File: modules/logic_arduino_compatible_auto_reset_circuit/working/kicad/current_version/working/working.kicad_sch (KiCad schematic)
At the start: 2 parts

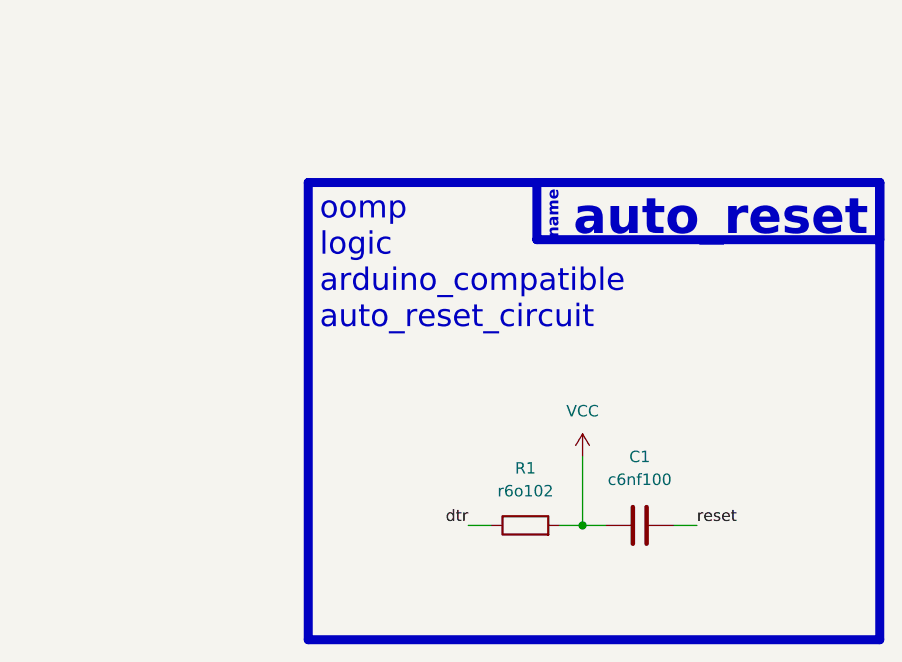
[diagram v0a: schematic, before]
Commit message: fixed formatting to be more consistent
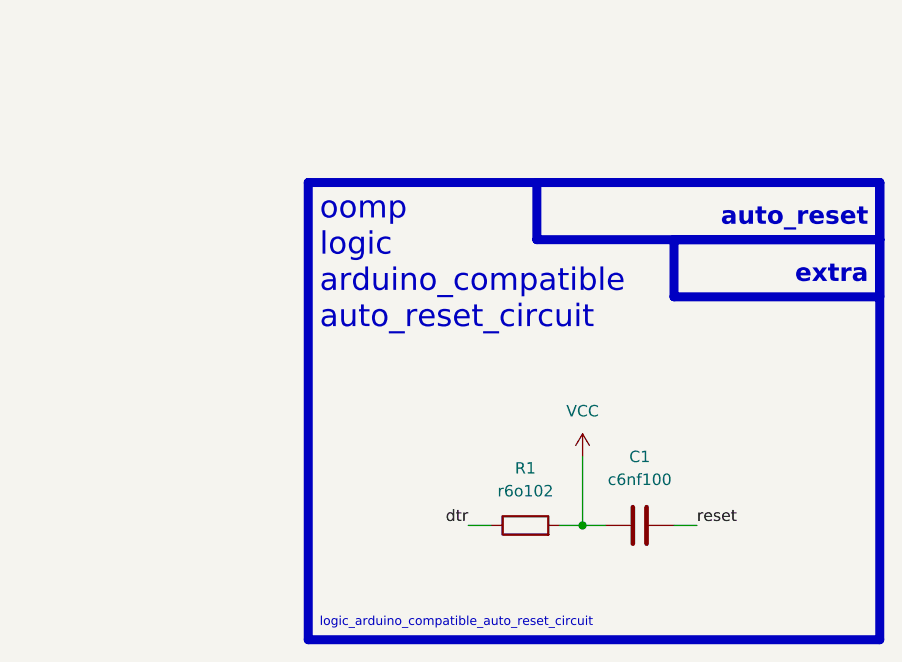
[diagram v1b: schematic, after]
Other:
- note added: "extra"
- note added: "logic_arduino_compatible_auto_reset_circuit"
- note removed: "name"
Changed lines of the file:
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@@
   (rectangle (start 127 57.15) (end 165.1 63.5)
     (stroke (width 1) (type default))
-    (fill (type color) (color 0 0 0 0))
+    (fill (type none))
   )
   (rectangle (start 101.6 57.15) (end 165.1 107.95)
@@
     (fill (type none))
   )
-  (text "auto_reset" (at 163.83 63.5 0)
-    (effects (font (size 4 4) (thickness 0.8) bold (color 255 255 255 1)) (justify right bottom))
+  (rectangle (start 142.24 63.5) (end 165.1 69.85)
+    (stroke (width 1) (type default))
+    (fill (type none))
   )
-  (text "name" (at 129.54 63.5 90)
-    (effects (font (size 1.27 1.27) (thickness 0.254) bold (color 255 255 255 1)) (justify left bottom))
+  (text "extra" (at 163.83 68.58 0)
+    (effects (font (size 2 2) (thickness 0.8) bold) (justify right bottom))
+  )
+  (text "auto_reset" (at 163.83 62.23 0)
+    (effects (font (size 2 2) (thickness 0.8) bold) (justify right bottom))
+  )
+  (text "logic_arduino_compatible_auto_reset_circuit" (at 102.87 106.68 0)
+    (effects (font (size 1 1)) (justify left bottom))
   )
   (text "oomp\nlogic\narduino_compatible\nauto_reset_circuit" (at 102.87 73.66 0)

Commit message: schematic formatting
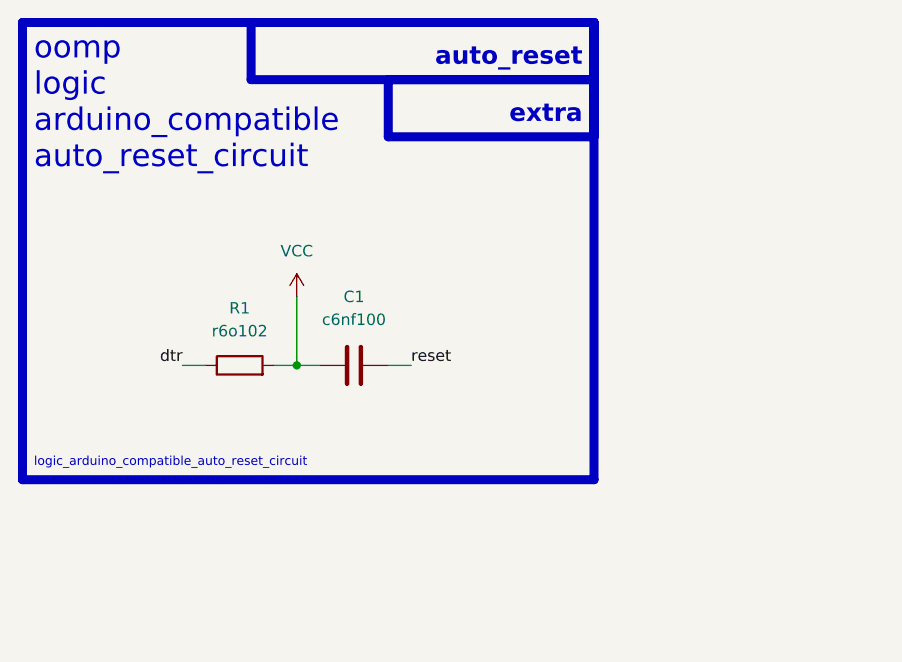
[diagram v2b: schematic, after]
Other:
- moved on the sheet: C1, R1
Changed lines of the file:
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@@
 (kicad_sch (version 20230121) (generator eeschema)
-  (paper "A4")
-  (junction (at 132.08 95.25) (diameter 0) (color 0 0 0 0)
+  (paper "A5")
+  (junction (at 100.33 77.47) (diameter 0) (color 0 0 0 0)
   )
-  (wire (pts (xy 132.08 95.25) (xy 129.54 95.25))
+  (wire (pts (xy 100.33 77.47) (xy 97.79 77.47))
     (stroke (width 0) (type default))
   )
-  (wire (pts (xy 132.08 95.25) (xy 134.62 95.25))
+  (wire (pts (xy 100.33 77.47) (xy 102.87 77.47))
     (stroke (width 0) (type default))
   )
-  (wire (pts (xy 142.24 95.25) (xy 144.78 95.25))
+  (wire (pts (xy 110.49 77.47) (xy 113.03 77.47))
     (stroke (width 0) (type default))
   )
-  (wire (pts (xy 119.38 95.25) (xy 121.92 95.25))
+  (wire (pts (xy 87.63 77.47) (xy 90.17 77.47))
     (stroke (width 0) (type default))
   )
-  (wire (pts (xy 132.08 87.63) (xy 132.08 95.25))
+  (wire (pts (xy 100.33 69.85) (xy 100.33 77.47))
     (stroke (width 0) (type default))
   )
-  (rectangle (start 127 57.15) (end 165.1 63.5)
+  (rectangle (start 95.25 39.37) (end 133.35 45.72)
     (stroke (width 1) (type default))
     (fill (type none))
   )
-  (rectangle (start 101.6 57.15) (end 165.1 107.95)
+  (rectangle (start 69.85 39.37) (end 133.35 90.17)
     (stroke (width 1) (type default))
     (fill (type none))
   )
-  (rectangle (start 142.24 63.5) (end 165.1 69.85)
+  (rectangle (start 110.49 45.72) (end 133.35 52.07)
     (stroke (width 1) (type default))
     (fill (type none))
   )
-  (text "extra" (at 163.83 68.58 0)
+  (text "extra" (at 132.08 50.8 0)
     (effects (font (size 2 2) (thickness 0.8) bold) (justify right bottom))
   )
-  (text "auto_reset" (at 163.83 62.23 0)
+  (text "auto_reset" (at 132.08 44.45 0)
     (effects (font (size 2 2) (thickness 0.8) bold) (justify right bottom))
   )
-  (text "logic_arduino_compatible_auto_reset_circuit" (at 102.87 106.68 0)
+  (text "logic_arduino_compatible_auto_reset_circuit" (at 71.12 88.9 0)
     (effects (font (size 1 1)) (justify left bottom))
   )
-  (text "oomp\nlogic\narduino_compatible\nauto_reset_circuit" (at 102.87 73.66 0)
+  (text "oomp\nlogic\narduino_compatible\nauto_reset_circuit" (at 71.12 55.88 0)
     (effects (font (size 2.5 2.5)) (justify left bottom))
   )
-  (label "dtr" (at 119.38 95.25 180) (fields_autoplaced)
+  (label "dtr" (at 87.63 77.47 180) (fields_autoplaced)
     (effects (font (size 1.27 1.27)) (justify right bottom))
   )
-  (label "reset" (at 144.78 95.25 0) (fields_autoplaced)
+  (label "reset" (at 113.03 77.47 0) (fields_autoplaced)
     (effects (font (size 1.27 1.27)) (justify left bottom))
   )
-  (symbol (lib_name "c6nf100_electronic_capacitor_0603_100_nano_farad_1") (lib_id "oomlout_oomp_part_symbols:c6nf100_electronic_capacitor_0603_100_nano_farad") (at 138.43 95.25 90) (unit 1)
+  (symbol (lib_name "c6nf100_electronic_capacitor_0603_100_nano_farad_1") (lib_id "oomlout_oomp_part_symbols:c6nf100_electronic_capacitor_0603_100_nano_farad") (at 106.68 77.47 90) (unit 1)
     (in_bom yes) (on_board yes) (dnp no) (fields_autoplaced)
-    (property "Reference" "C1" (at 138.43 87.63 90)
+    (property "Reference" "C1" (at 106.68 69.85 90)
       (effects (font (size 1.27 1.27)))
     )
-    (property "Value" "c6nf100" (at 138.43 90.17 90)
+    (property "Value" "c6nf100" (at 106.68 72.39 90)
       (effects (font (size 1.27 1.27)))
     )
-    (property "Footprint" "oomlout_oomp_part_footprints:c6nf100_electronic_capacitor_0603_100_nano_farad" (at 142.24 94.2848 0)
+    (property "Footprint" "oomlout_oomp_part_footprints:c6nf100_electronic_capacitor_0603_100_nano_farad" (at 110.49 76.5048 0)
       (effects (font (size 1.27 1.27)) hide)
     )
-    (property "Datasheet" "https://github.com/oomlout/oomlout_oomp_v3/parts/electronic_capacitor_0603_100_nano_farad/datasheet.pdf" (at 138.43 95.25 0)
+    (property "Datasheet" "https://github.com/oomlout/oomlout_oomp_v3/parts/electronic_capacitor_0603_100_nano_farad/datasheet.pdf" (at 106.68 77.47 0)
       (effects (font (size 1.27 1.27)) hide)
     )
@@
     )
   )
-  (symbol (lib_id "oomlout_oomp_part_symbols:r6o102_electronic_resistor_0603_1000_ohm") (at 125.73 95.25 90) (unit 1)
+  (symbol (lib_id "oomlout_oomp_part_symbols:r6o102_electronic_resistor_0603_1000_ohm") (at 93.98 77.47 90) (unit 1)
     (in_bom yes) (on_board yes) (dnp no) (fields_autoplaced)
-    (property "Reference" "R1" (at 125.73 88.9 90)
+    (property "Reference" "R1" (at 93.98 71.12 90)
       (effects (font (size 1.27 1.27)))
     )
-    (property "Value" "r6o102" (at 125.73 91.44 90)
+    (property "Value" "r6o102" (at 93.98 73.66 90)
       (effects (font (size 1.27 1.27)))
     )
-    (property "Footprint" "oomlout_oomp_part_footprints:r6o102_electronic_resistor_0603_1000_ohm" (at 125.73 97.028 90)
+    (property "Footprint" "oomlout_oomp_part_footprints:r6o102_electronic_resistor_0603_1000_ohm" (at 93.98 79.248 90)
       (effects (font (size 1.27 1.27)) hide)
     )
-    (property "Datasheet" "https://github.com/oomlout/oomlout_oomp_v3/parts/electronic_resistor_0603_1000_ohm/datasheet.pdf" (at 125.73 95.25 0)
+    (property "Datasheet" "https://github.com/oomlout/oomlout_oomp_v3/parts/electronic_resistor_0603_1000_ohm/datasheet.pdf" (at 93.98 77.47 0)
       (effects (font (size 1.27 1.27)) hide)
     )
@@
     )
   )
-  (symbol (lib_id "power:VCC") (at 132.08 87.63 0) (unit 1)
+  (symbol (lib_id "power:VCC") (at 100.33 69.85 0) (unit 1)
     (in_bom yes) (on_board yes) (dnp no) (fields_autoplaced)
-    (property "Reference" "#PWR01" (at 132.08 91.44 0)
+    (property "Reference" "#PWR01" (at 100.33 73.66 0)
       (effects (font (size 1.27 1.27)) hide)
     )
-    (property "Value" "VCC" (at 132.08 82.55 0)
+    (property "Value" "VCC" (at 100.33 64.77 0)
       (effects (font (size 1.27 1.27)))
     )
-    (property "Footprint" "" (at 132.08 87.63 0)
+    (property "Footprint" "" (at 100.33 69.85 0)
       (effects (font (size 1.27 1.27)) hide)
     )
-    (property "Datasheet" "" (at 132.08 87.63 0)
+    (property "Datasheet" "" (at 100.33 69.85 0)
       (effects (font (size 1.27 1.27)) hide)
     )
